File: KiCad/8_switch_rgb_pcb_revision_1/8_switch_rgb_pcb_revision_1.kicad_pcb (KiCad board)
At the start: 2 copper layers, 100 x 100 mm, 110 parts, among them SW0 SW0, SW1 SW1, SW2 SW2, SW3 SW3, SW4 SW4, SW5 SW5, SW6 SW6, SW7 SW7, U2 74HC165, Y1 16MHz

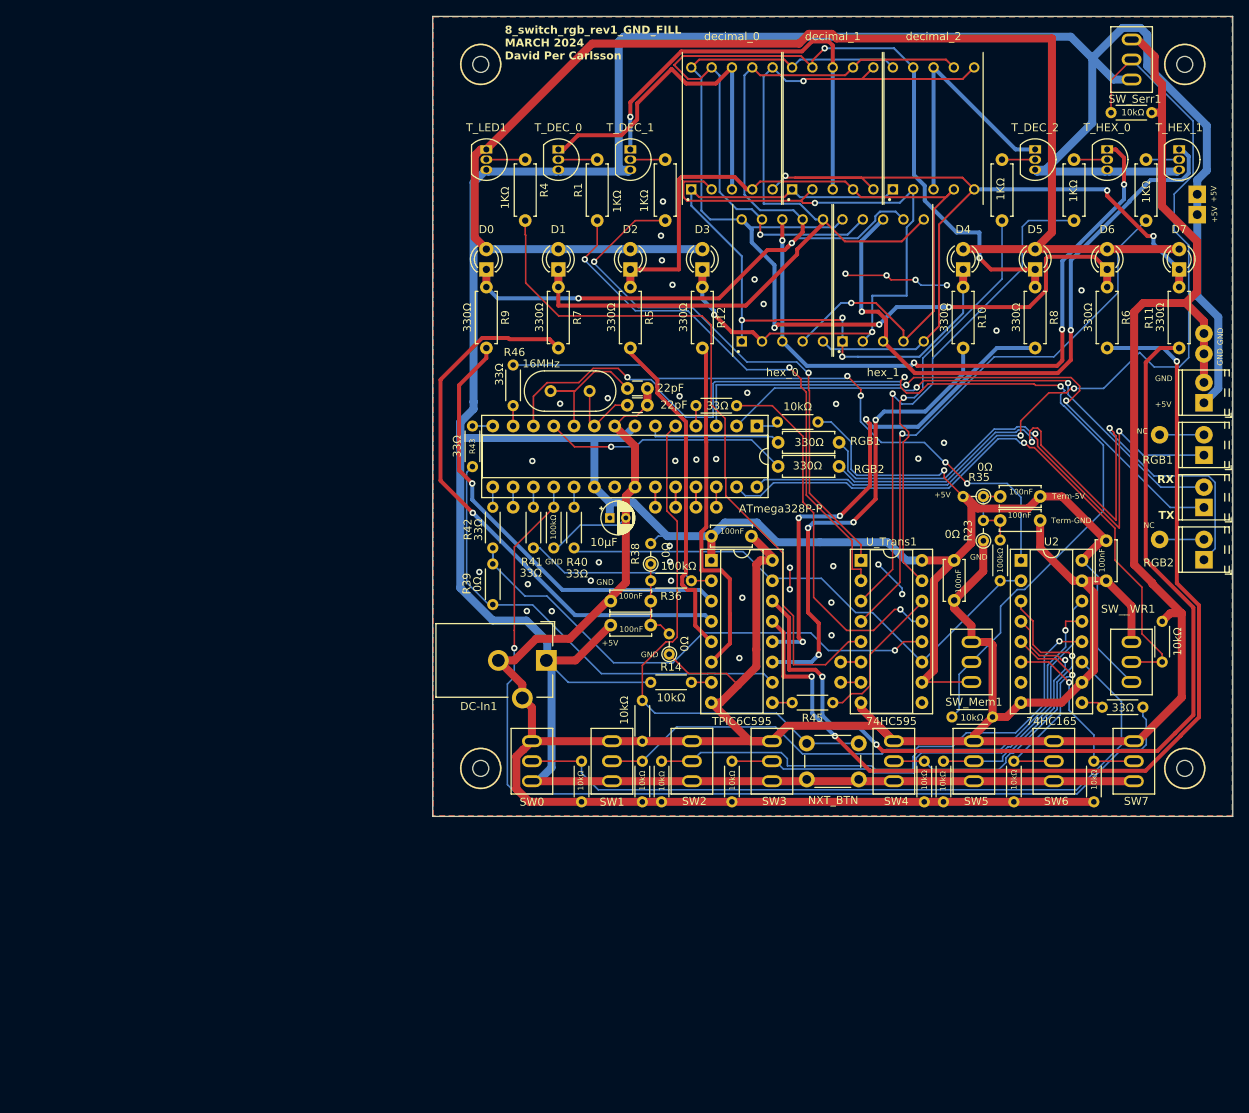
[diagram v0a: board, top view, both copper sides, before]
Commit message: Added some PDFs Realized the distance between the data line and the gnd for the pulldown resistor for data in from the 74hc165 is way too small, but can't do nothing about that now. It is two different stages, the data out from the 74hc165 should be low. Hopefully the pulldown resistor for data in isn't even needed, so it is litterally gnd-plane.
Still ugly 45+45 degree angle within 2mm
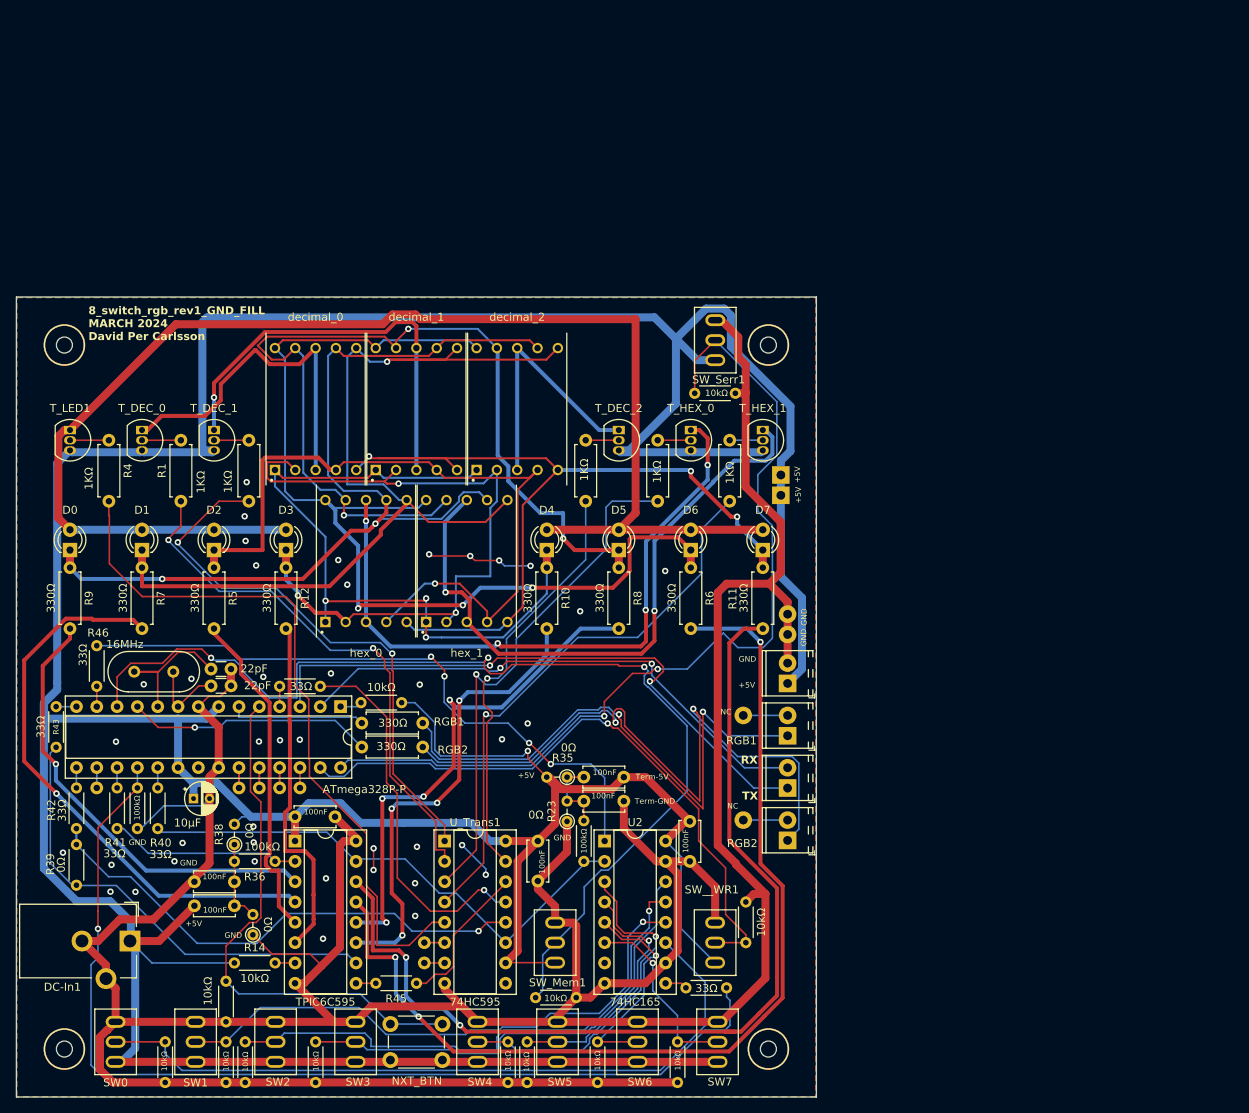
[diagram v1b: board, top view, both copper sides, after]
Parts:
- moved R26 62.8 mm to (140.2, 99.5)
- moved C1 62.8 mm to (82.3, 136.1)
- moved R15 62.8 mm to (81.6, 173.0)
- moved R31 62.8 mm to (84.0, 180.6)
- moved R32 62.8 mm to (81.6, 180.6)
- moved R35 62.8 mm to (124.3, 147.5)
- moved R36 62.8 mm to (87.8, 158.0)
- moved SW_Mem1 62.8 mm to (123.1, 168.1)
- moved ? 62.8 mm to (65.5, 148.8)
- moved ? 62.8 mm to (106.4, 170.7)
- moved ? 62.8 mm to (83.3, 148.8)
- moved ? 62.8 mm to (106.4, 168.2)
- moved ? 62.8 mm to (90.9, 148.8)
- moved ? 62.8 mm to (146.3, 152.9)
- moved CU_BUTTONS1 62.8 mm to (139.6, 158.0)
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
